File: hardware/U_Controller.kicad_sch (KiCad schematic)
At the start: 0 parts

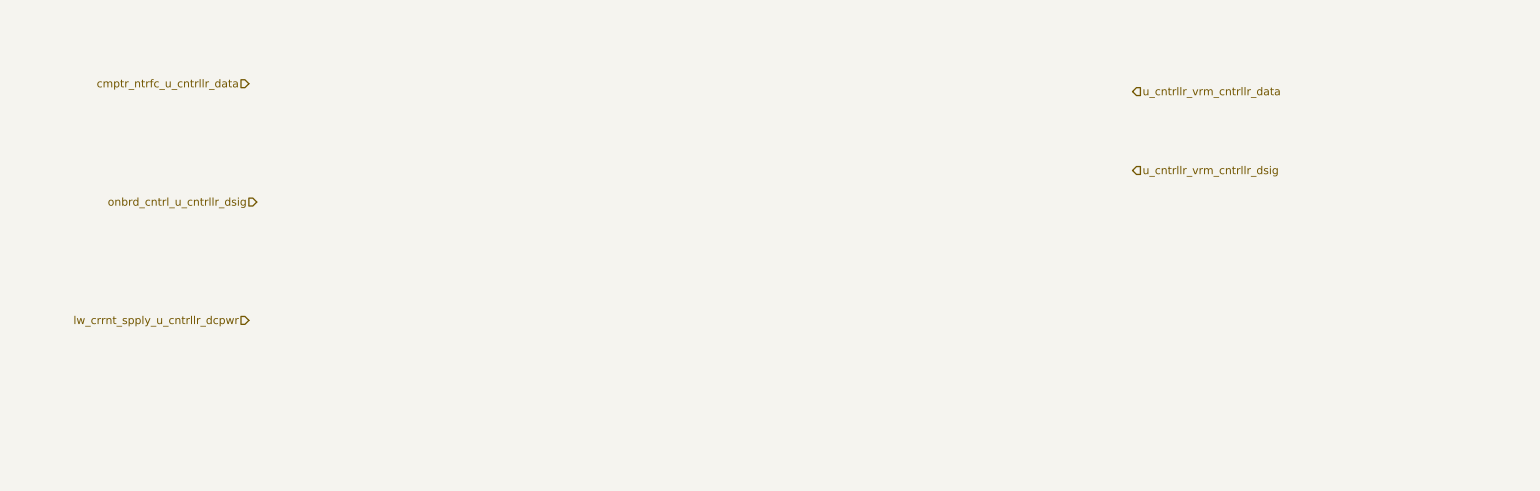
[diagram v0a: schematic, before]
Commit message: feat: microcontroller on the PCB
Added the microcontroller and made some basic connections
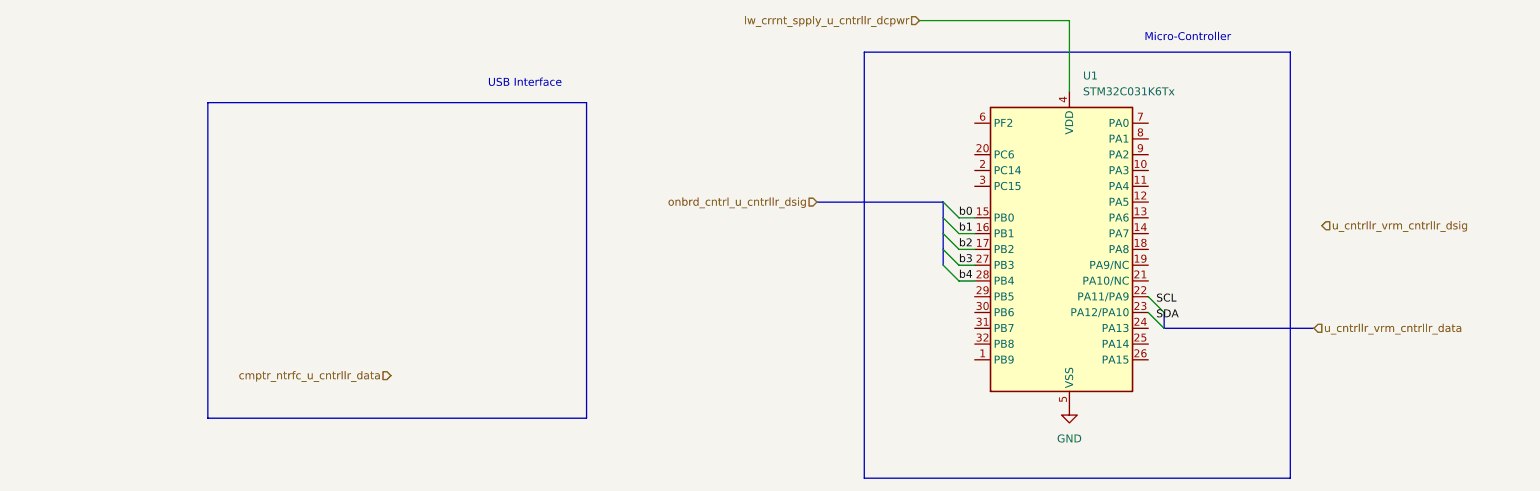
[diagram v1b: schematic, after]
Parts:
- added U1: STM32C031K6Tx, Package_QFP:LQFP-32_7x7mm_P0.8mm, symbol MCU_ST_STM32C0:STM32C031K6Tx
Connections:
- net lw_crrnt_spply_u_cntrllr_dcpwr: now also U1.4 (VDD)
- new net GND: U1.5 (VSS)
- new net b0: U1.15 (PB0)
- new net b1: U1.16 (PB1)
- new net b2: U1.17 (PB2)
- new net b3: U1.27 (PB3)
- new net b4: U1.28 (PB4)
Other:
- note added: "Micro-Controller"
- note added: "USB Interface"

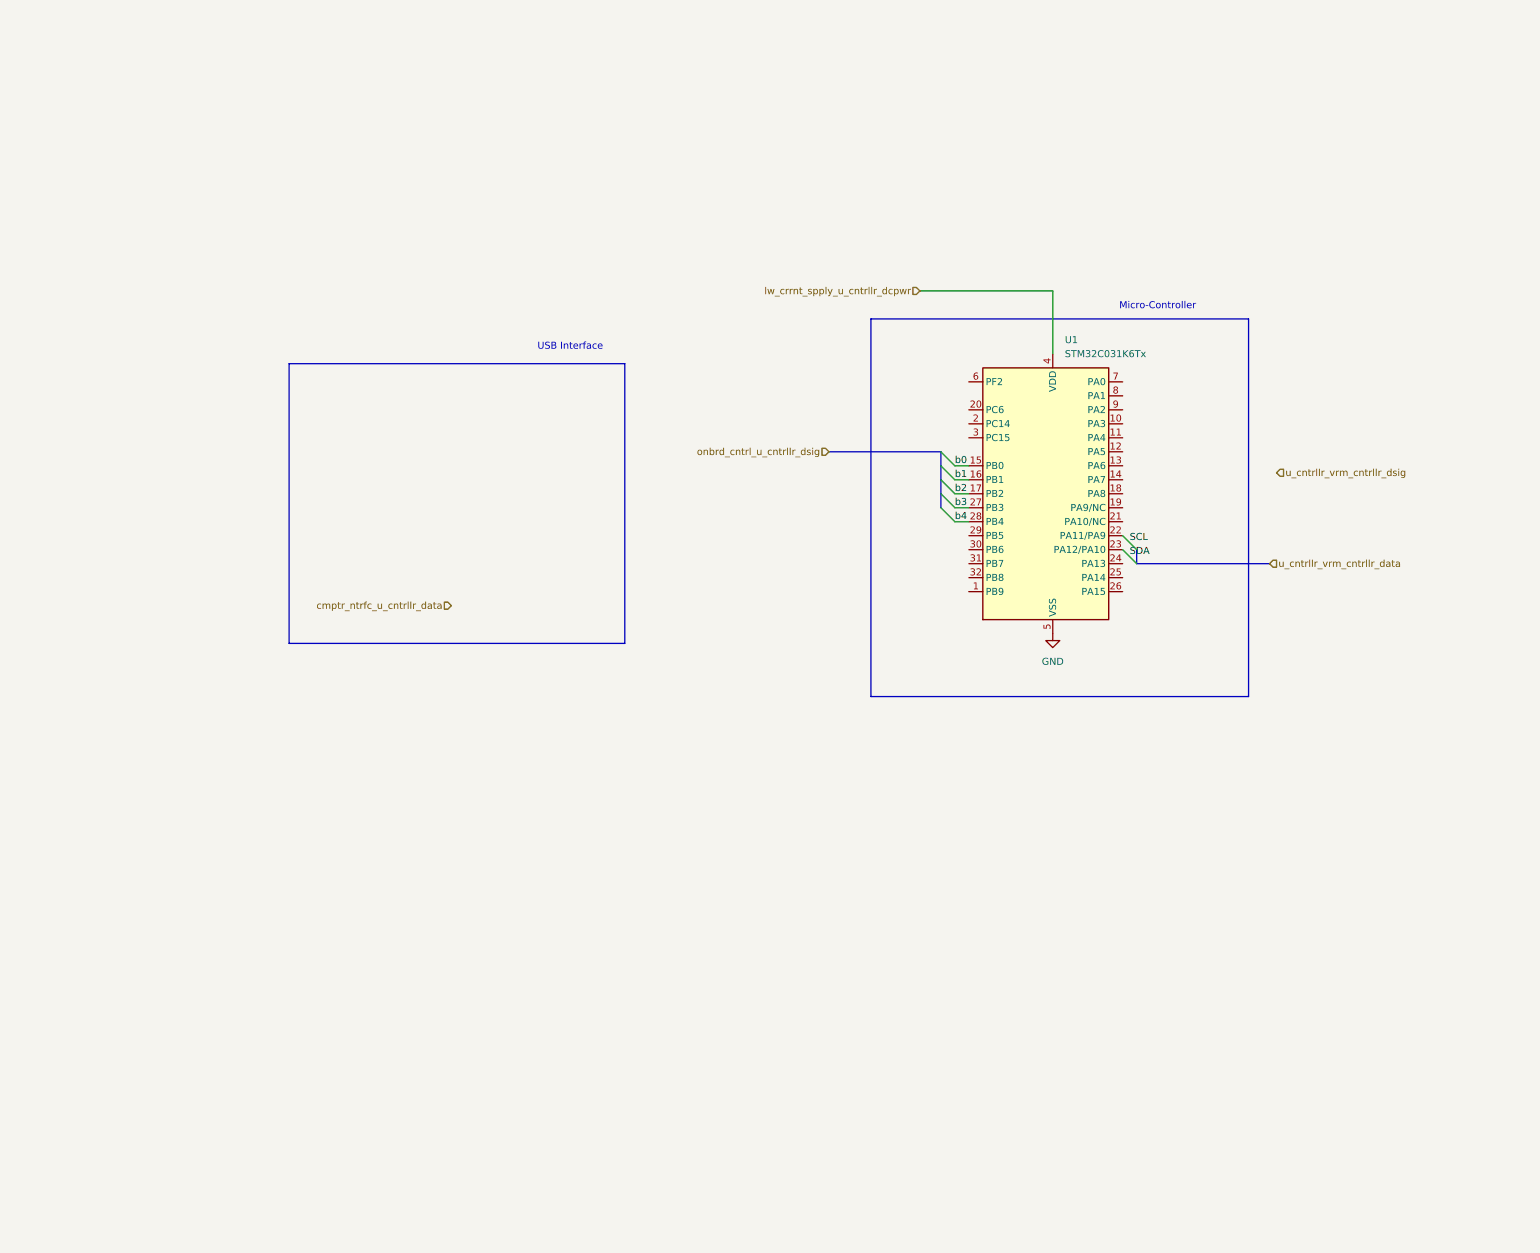
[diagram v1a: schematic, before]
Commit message: feat: USB-C Port and init of stm32c071
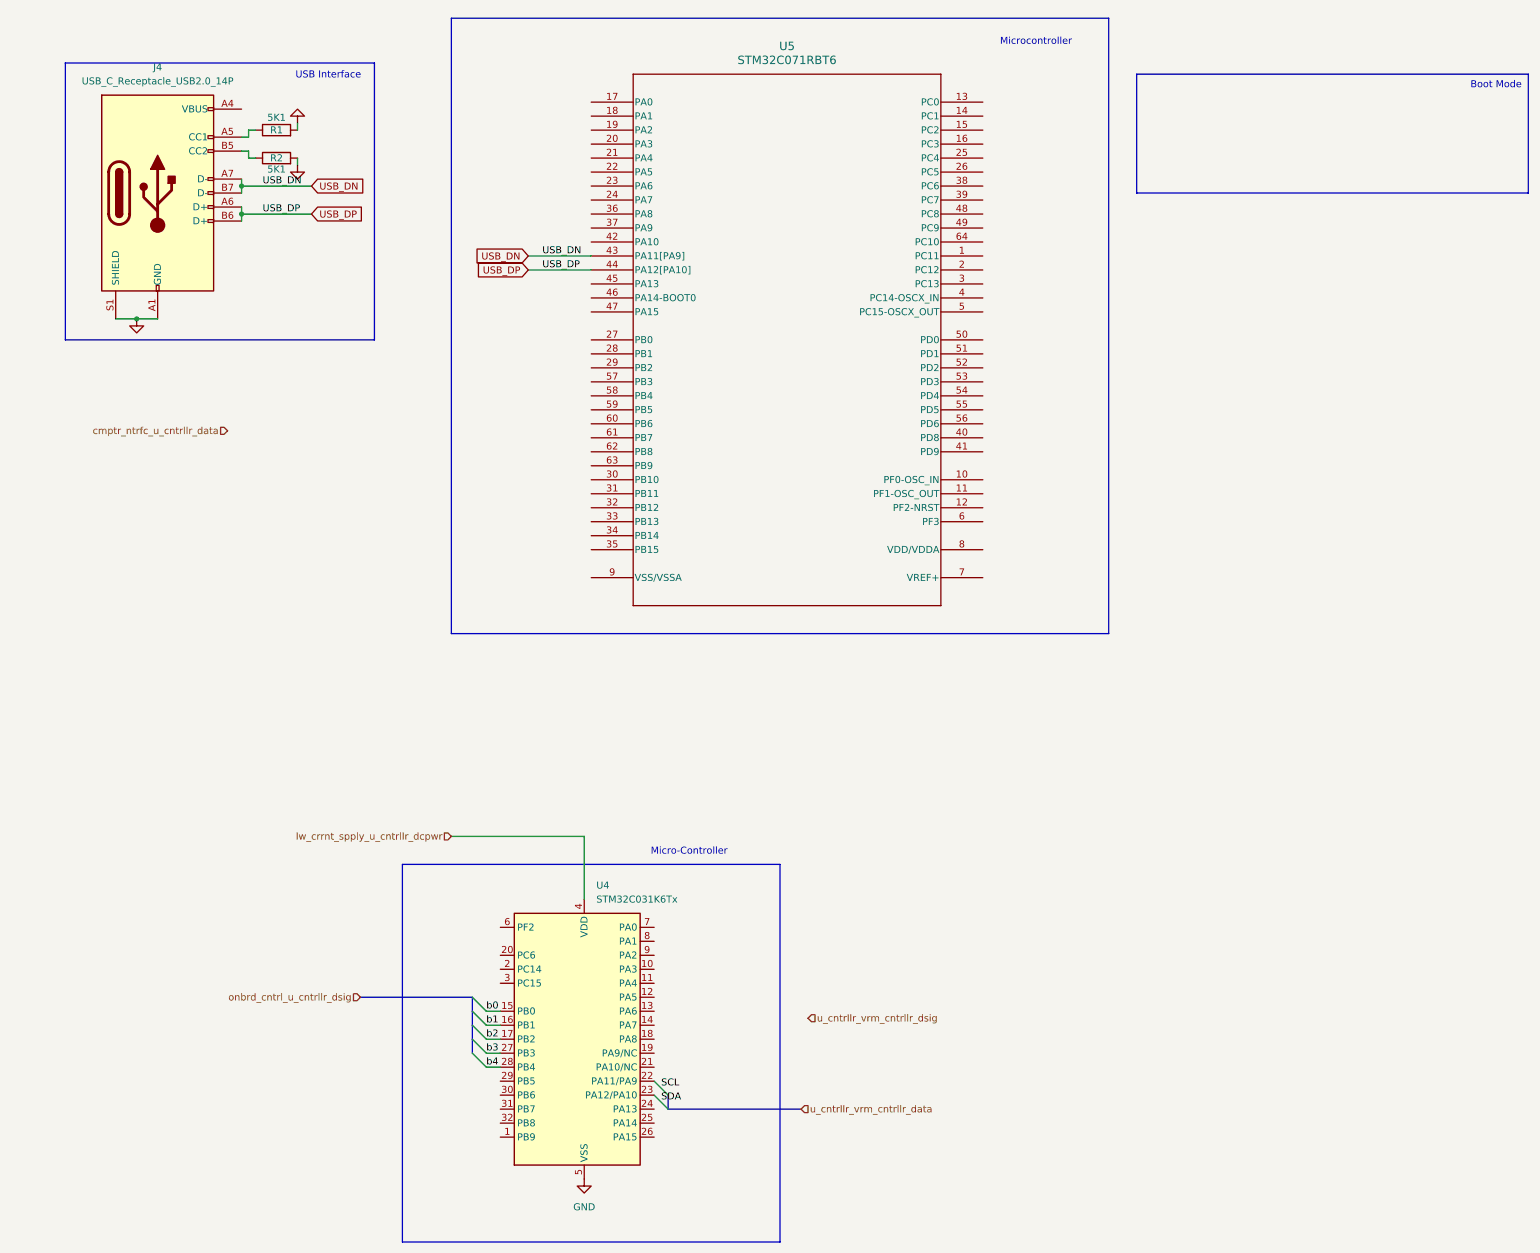
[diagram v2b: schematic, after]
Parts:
- added J4: USB_C_Receptacle_USB2.0_14P, symbol Connector:USB_C_Receptacle_USB2.0_14P
- added R1, R2: 5K1, symbol Device:R
- added U5: STM32C071RBT6, LQFP-64_STM, symbol Symbol_Library:STM32C071RBT6
- renumbered U1 to U4
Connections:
- net GND: now also J4.A1 (GND), J4.A12 (GND), J4.B1 (GND), J4.B12 (GND), J4.S1 (SHIELD), R1.2, R2.2
- new net: J4.B5 (CC2), R2.1
- new net: J4.A4 (VBUS), J4.A9 (VBUS), J4.B4 (VBUS), J4.B9 (VBUS)
- new net: J4.A5 (CC1), R1.1
- new net USB_DN: J4.A7 (D-), J4.B7 (D-), U5.43 (PA11[PA9])
- new net USB_DP: J4.A6 (D+), J4.B6 (D+), U5.44 (PA12[PA10])
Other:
- note added: "Boot Mode"
- note added: "Microcontroller"
- moved on the sheet: U4

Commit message: feat(schematic): USB on microcontroller
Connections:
- net GND: now also U5.8 (VDD/VDDA)
- net lw_crrnt_spply_u_cntrllr_dcpwr: now also U5.9 (VSS/VSSA); no longer U4.4 (VDD)
- net NRST: now reaches U5.12 (PF2-NRST)
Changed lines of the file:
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@@
+	(wire
+		(pts
+			(xy 85.09 116.84) (xy 113.03 116.84)
+		)
+		(stroke
+			(width 0)
+			(type default)
+		)
+	)
 	(wire
 		(pts
@@
 	(wire
 		(pts
+			(xy 187.96 130.81) (xy 187.96 111.76)
+		)
+		(stroke
+			(width 0)
+			(type default)
+		)
+	)
+	(wire
+		(pts
 			(xy 49.53 49.53) (xy 49.53 50.8)
 		)
@@
 	(wire
 		(pts
-			(xy 111.76 163.83) (xy 111.76 175.26)
-		)
-		(stroke
-			(width 0)
-			(type default)
-		)
-	)
-	(wire
-		(pts
 			(xy 93.98 198.12) (xy 96.52 198.12)
 		)
@@
 	(wire
 		(pts
+			(xy 187.96 111.76) (xy 184.15 111.76)
+		)
+		(stroke
+			(width 0)
+			(type default)
+		)
+	)
+	(wire
+		(pts
 			(xy 50.8 35.56) (xy 52.07 35.56)
 		)
@@
 	(wire
 		(pts
+			(xy 184.15 104.14) (xy 191.77 104.14)
+		)
+		(stroke
+			(width 0)
+			(type default)
+		)
+	)
+	(wire
+		(pts
 			(xy 93.98 203.2) (xy 96.52 203.2)
 		)
@@
 		(pts
 			(xy 127 213.36) (xy 151.13 213.36)
-		)
-		(stroke
-			(width 0)
-			(type default)
-		)
-	)
-	(wire
-		(pts
-			(xy 87.63 163.83) (xy 111.76 163.83)
 		)
 		(stroke
@@
 		)
 	)
+	(label "NRST"
+		(at 185.42 104.14 0)
+		(fields_autoplaced yes)
+		(effects
+			(font
+				(size 1.27 1.27)
+			)
+			(justify left bottom)
+		)
+	)
 	(label "b0"
 		(at 93.98 195.58 0)
@@
 		)
 	)
+	(global_label "NRST"
+		(shape input)
+		(at 191.77 104.14 0)
+		(fields_autoplaced yes)
+		(effects
+			(font
+				(size 1.27 1.27)
+			)
+			(justify left)
+		)
+		(property "Intersheetrefs" "${INTERSHEET_REFS}"
+			(at 199.5328 104.14 0)
+			(effects
+				(font
+					(size 1.27 1.27)
+				)
+				(justify left)
+				(hide yes)
+			)
+		)
+	)
 	(global_label "USB_DN"
 		(shape input)
@@
 	(hierarchical_label "lw_crrnt_spply_u_cntrllr_dcpwr"
 		(shape input)
-		(at 87.63 163.83 180)
+		(at 85.09 116.84 180)
 		(fields_autoplaced yes)
 		(effects
@@
 					(unit 1)
 				)
+			)
+		)
+	)
+	(symbol
+		(lib_id "power:GND")
+		(at 187.96 130.81 0)
+		(unit 1)
+		(exclude_from_sim no)
+		(in_bom yes)
+		(on_board yes)
+		(dnp no)
+		(fields_autoplaced yes)
+		(property "Reference" "#PWR044"
+			(at 187.96 137.16 0)
+			(effects
+				(font
+					(size 1.27 1.27)
+				)
+				(hide yes)
+			)
+		)
+		(property "Value" "GND"
+			(at 187.96 135.89 0)
+			(effects
+				(font
+					(size 1.27 1.27)
+				)
+				(hide yes)
+			)
+		)
+		(property "Footprint" ""
+			(at 187.96 130.81 0)
+			(effects
+				(font
+					(size 1.27 1.27)
+				)
+				(hide yes)
+			)
+		)
+		(property "Datasheet" ""
+			(at 187.96 130.81 0)
+			(effects
+				(font
+					(size 1.27 1.27)
+				)
+				(hide yes)
+			)
+		)
+		(property "Description" "Power symbol creates a global label with name \"GND\" , ground"
+			(at 187.96 130.81 0)
+			(effects
+				(font
+					(size 1.27 1.27)
+				)
+				(hide yes)
+			)
+		)
+		(pin "1"
+		)
+		(instances
+			(project ""
+				(path "/d5303413-7068-41ba-88e3-39dfa38d31b7/027ff087-ab1d-45e5-9d8f-c94102656fe5"
+					(reference "#PWR044")
+					(unit 1)
+				)
